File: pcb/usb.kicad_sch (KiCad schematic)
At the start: 38 parts, among them J6 USB4105, J7 S2B-PH-SM4-TB, Q1 DMG3401LSN, Q2 DMG3418L, Q3 DMG3418L, SW1 PBH2UEESNPNAGX, U149 SN74LVC2G132DCUR, U151 AP2112K-3.3, U152 BQ297xy, U153 MCP73831-2-OT

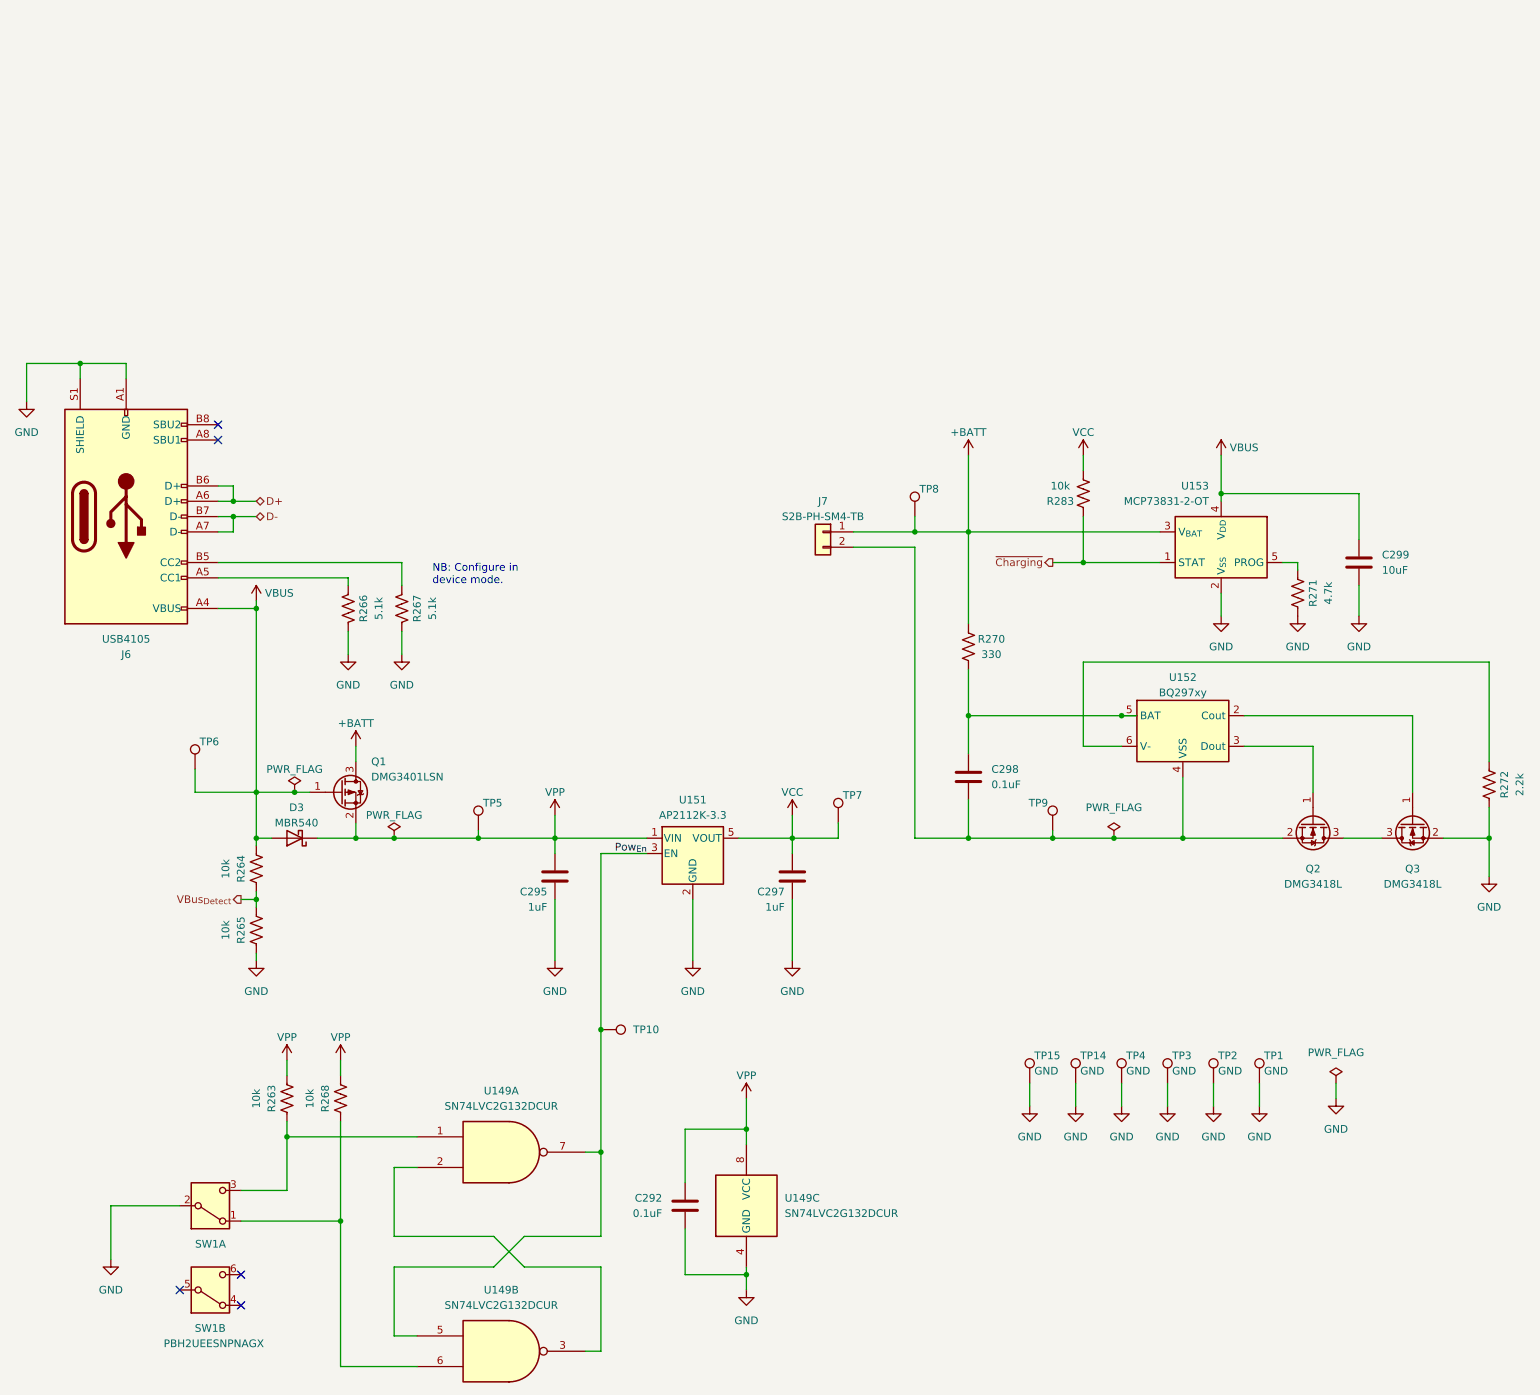
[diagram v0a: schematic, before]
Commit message: Rev. A of PCB
- I will make a case before fabrication so that they can be made
  together
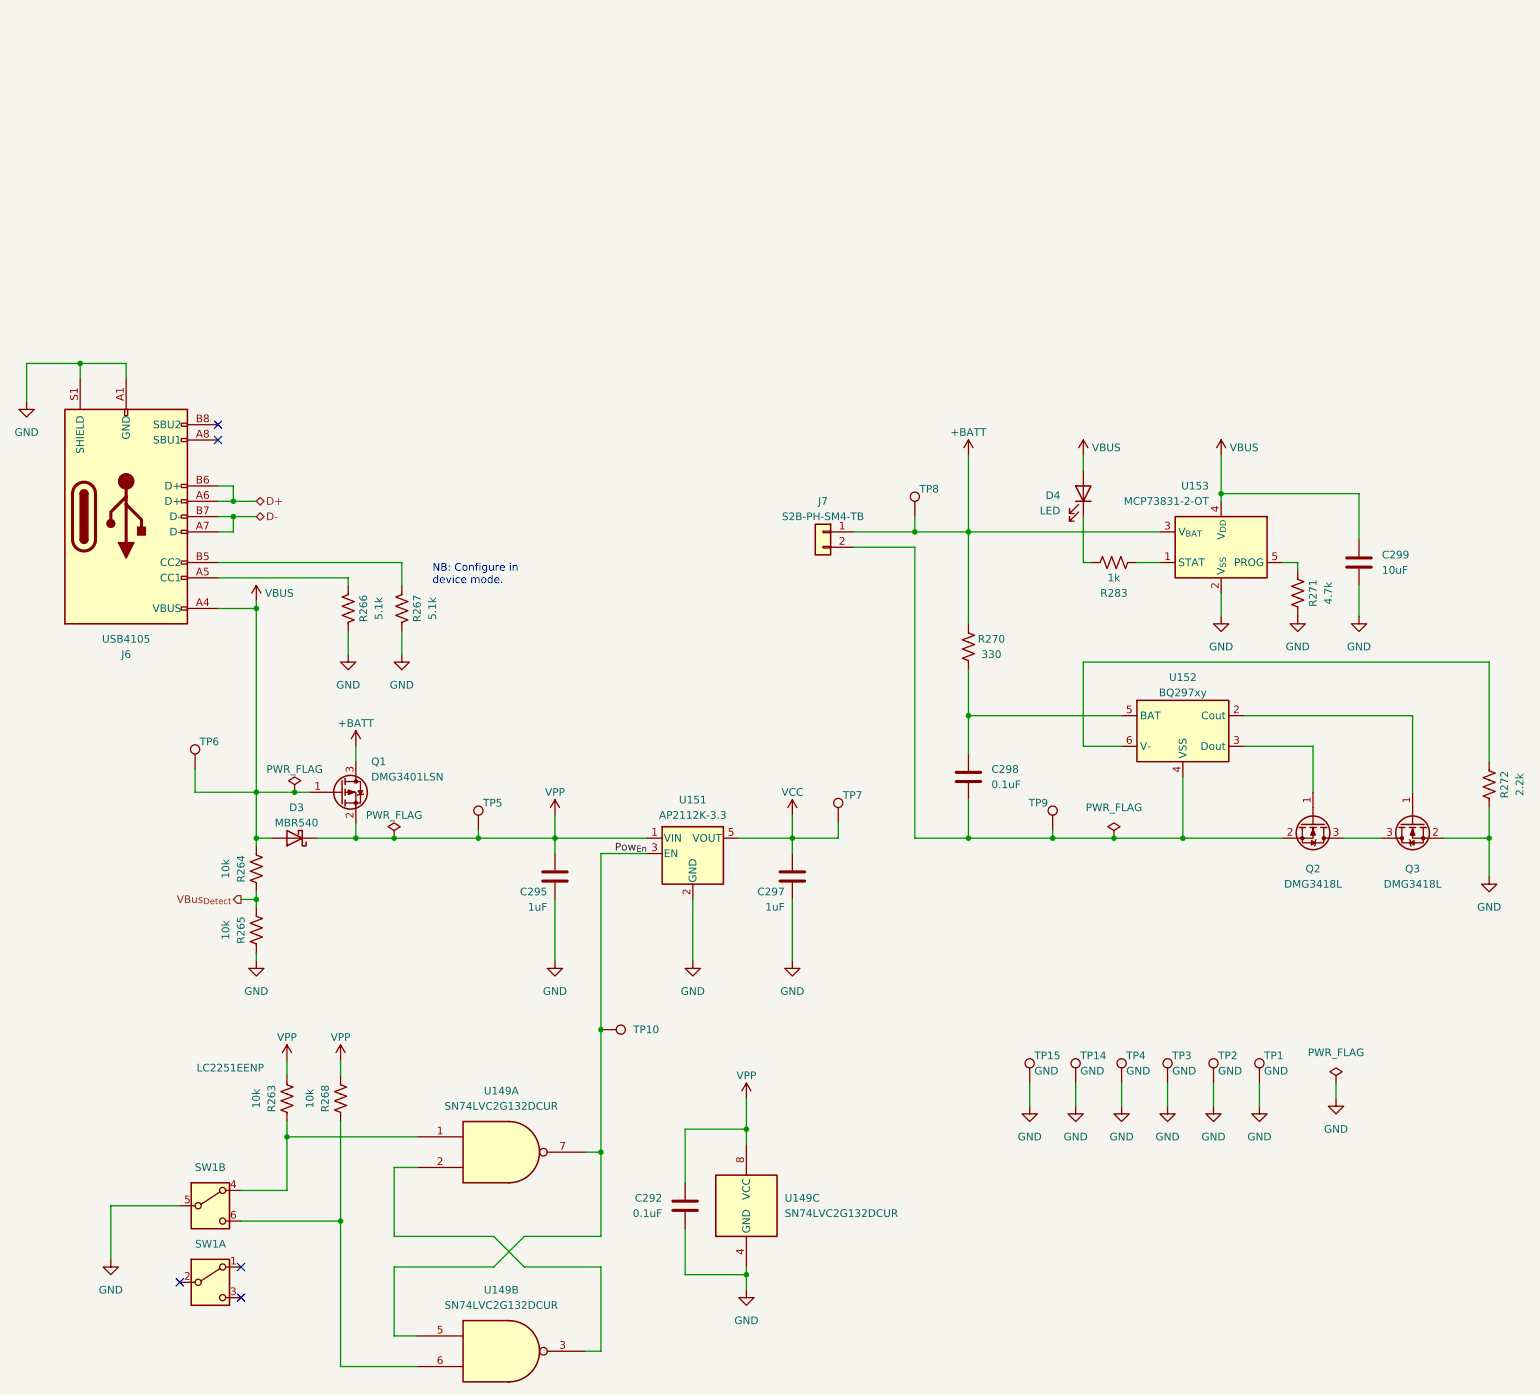
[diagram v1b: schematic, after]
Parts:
- added D4: LED, open-ephys:KINGBRIGHT_WP934CBGD, symbol Device:LED
- R283: value 10k -> 1k
- SW1: value PBH2UEESNPNAGX -> LC2251EENP; footprint open-ephys:ESWITCH_PBH2UxxNAGX -> open-ephys:ESWITCH_LC2251EENP
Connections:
- net GND: now also SW1.5 (B); no longer SW1.2 (B)
- net VBUS: now also D4.2 (A)
- net VCC: no longer R283.1
- net at R268.2, U149.6: now also SW1.6 (C); no longer SW1.1 (A)
- net at SW1.4 (A): now also R263.2, U149.1
- net ~{Charging}: no longer names the net of R283.2, U153.1 (STAT)
- new net: D4.1 (K), R283.1
- now unconnected: SW1.3 (C)
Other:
- moved on the sheet: R283

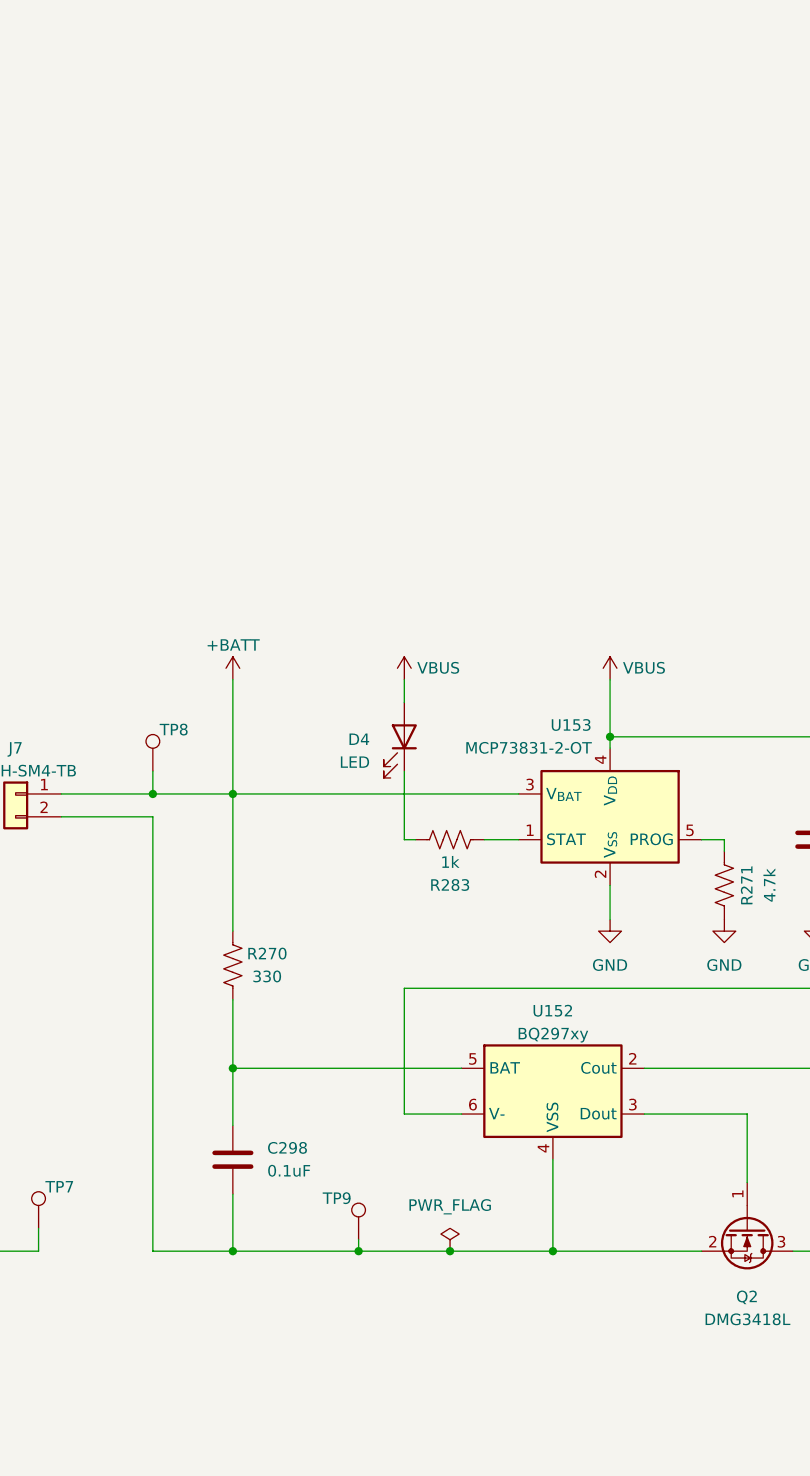
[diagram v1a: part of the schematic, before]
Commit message: Created case
- Mill aluminum
- Moved some components for more sensical layout for the user
- Pending final check, should be ready for initial fab
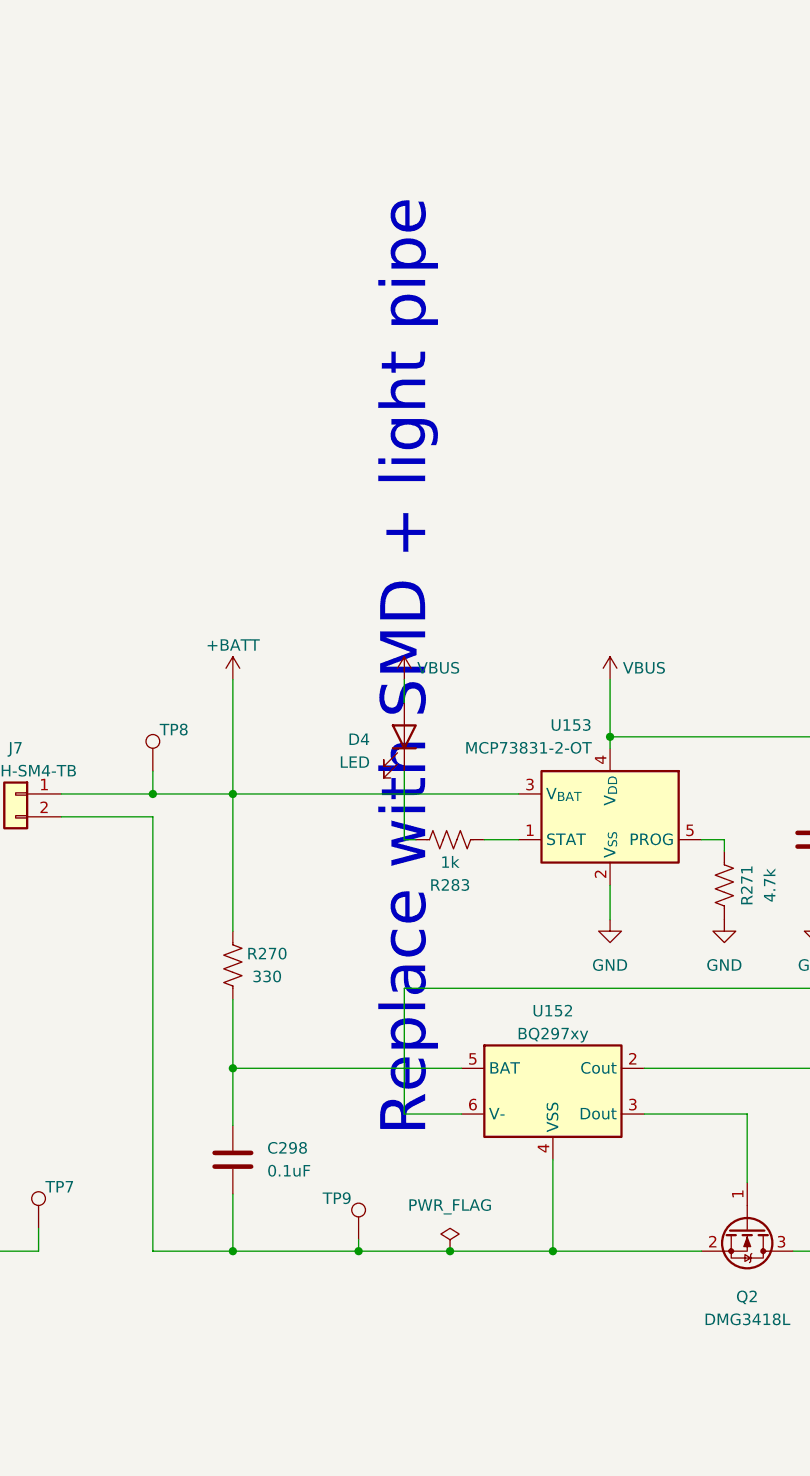
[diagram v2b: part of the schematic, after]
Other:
- note added: "Replace with SMD + light pipe"
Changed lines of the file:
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@@
+		)
+	)
+	(text "Replace with SMD + light pipe"
+		(exclude_from_sim no)
+		(at 205.74 35.56 90)
+		(effects
+			(font
+				(size 5 5)
+			)
 		)
 	)

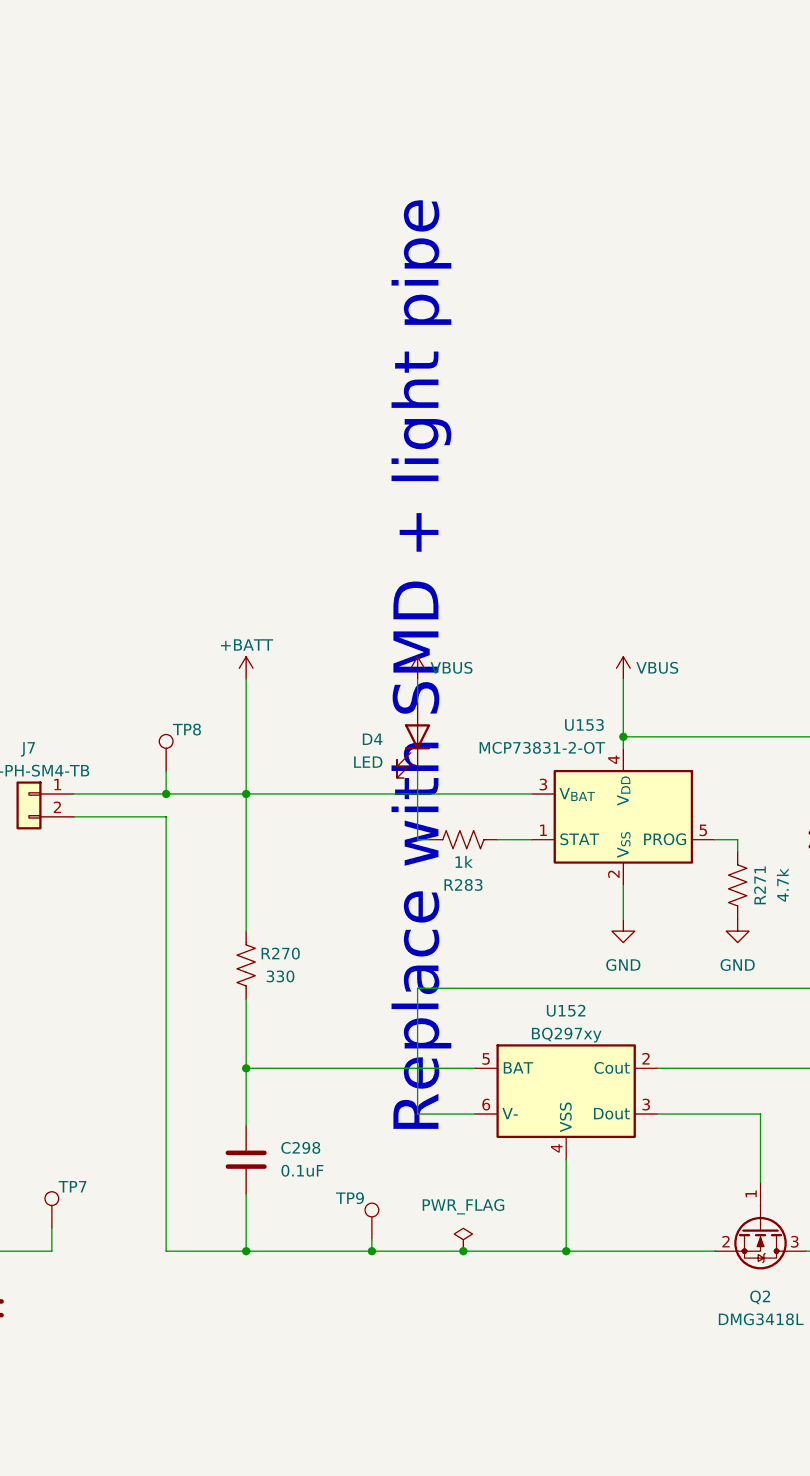
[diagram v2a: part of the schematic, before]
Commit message: Improved manufacturability of case design
- Quote request sent to PCBWay for this design along with the case
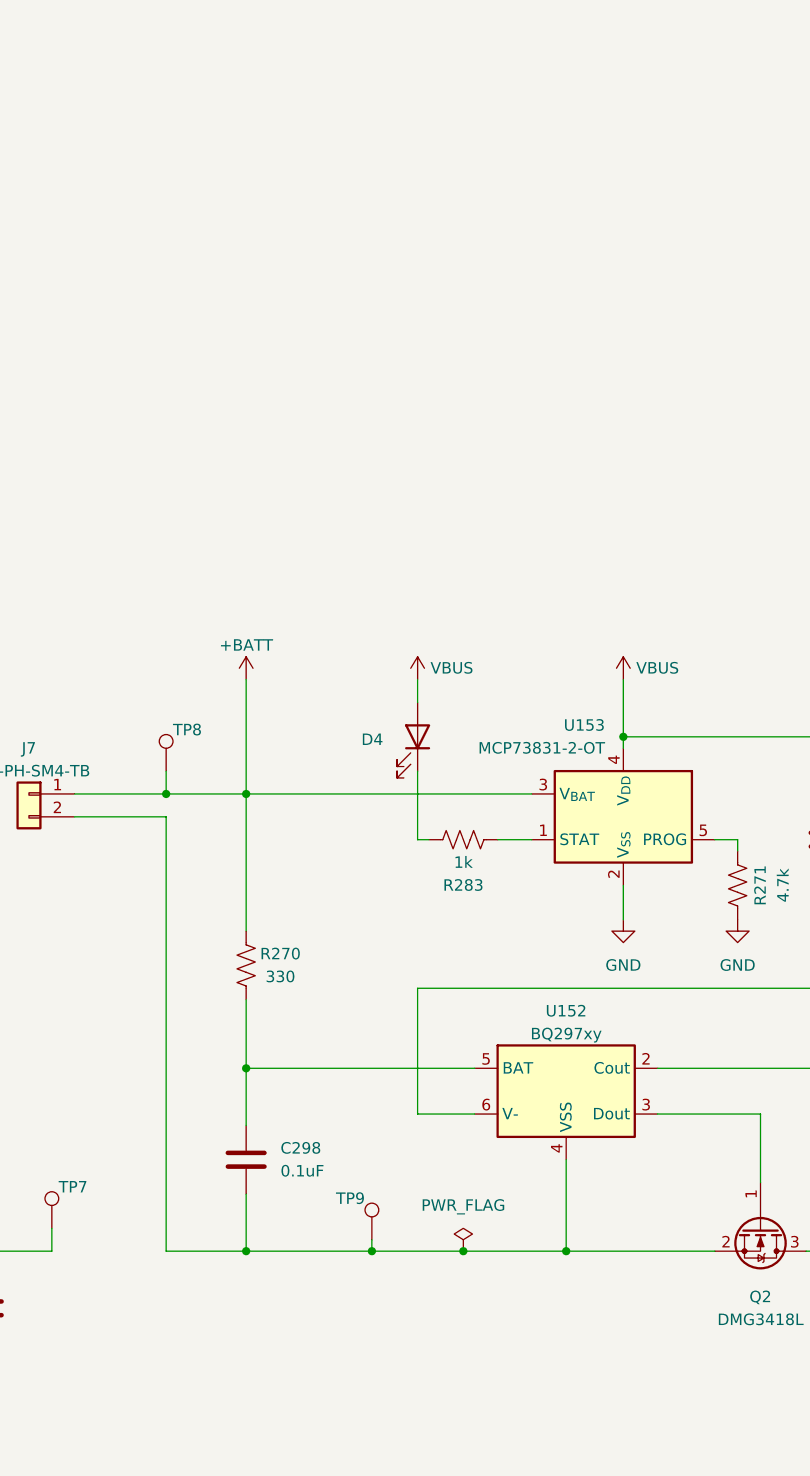
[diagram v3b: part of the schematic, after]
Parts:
- D4: footprint open-ephys:KINGBRIGHT_WP934CBGD -> LED_SMD:LED_0603_1608Metric
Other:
- note removed: "Replace with SMD + light pipe"
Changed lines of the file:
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@@
-		)
-	)
-	(text "Replace with SMD + light pipe"
-		(exclude_from_sim no)
-		(at 205.74 35.56 90)
-		(effects
-			(font
-				(size 5 5)
-			)
 		)
 	)
@@
 				)
 				(justify right)
-			)
-		)
-		(property "Footprint" "open-ephys:KINGBRIGHT_WP934CBGD"
+				(hide yes)
+			)
+		)
+		(property "Footprint" "LED_SMD:LED_0603_1608Metric"
 			(at 205.74 43.18 0)
 			(effects
